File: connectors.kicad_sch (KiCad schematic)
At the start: 4 parts, among them J1 Conn_01x05_Pin, J2 Conn_01x05_Pin, J3 Conn_01x09_Pin, J4 Conn_02x03_Odd_Even

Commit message: Values Added
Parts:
- renumbered J3 to J2, J2 to J3
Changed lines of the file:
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@@
 		(on_board yes)
 		(dnp no)
-		(property "Reference" "J3"
+		(property "Reference" "J2"
 			(at 112.395 99.06 0)
 			(effects
@@
 			(project ""
 				(path "/9a58bdc0-cf43-4f46-bdf9-3019f1d018de/dbde1bf3-31e8-43a9-a1f1-c0653e04f173"
-					(reference "J3")
+					(reference "J2")
 					(unit 1)
 				)
@@
 		(on_board yes)
 		(dnp no)
-		(property "Reference" "J2"
+		(property "Reference" "J3"
 			(at 131.445 72.39 0)
 			(effects
@@
 			(project "MCU_Datalogger"
 				(path "/9a58bdc0-cf43-4f46-bdf9-3019f1d018de/dbde1bf3-31e8-43a9-a1f1-c0653e04f173"
-					(reference "J2")
+					(reference "J3")
 					(unit 1)
 				)

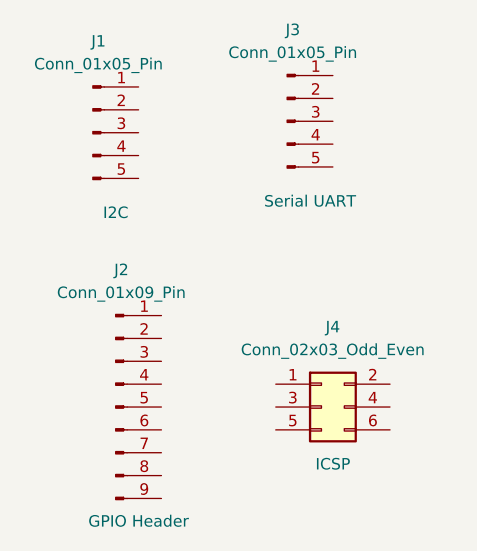
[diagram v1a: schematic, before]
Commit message: Problems in connectors fixed
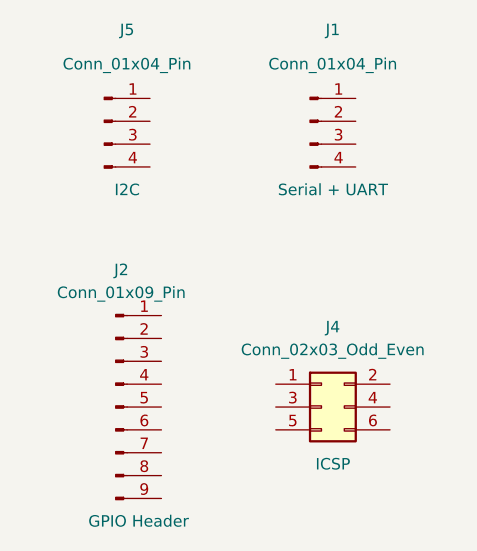
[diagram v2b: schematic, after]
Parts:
- removed J1, J3: Conn_01x05_Pin, symbol Connector:Conn_01x05_Pin
- added J1, J5: Conn_01x04_Pin, symbol Connector:Conn_01x04_Pin
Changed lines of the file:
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@@
+	)
+	(symbol
+		(lib_id "Connector:Conn_01x04_Pin")
+		(at 133.35 82.55 0)
+		(unit 1)
+		(exclude_from_sim no)
+		(in_bom yes)
+		(on_board yes)
+		(dnp no)
+		(property "Reference" "J1"
+			(at 135.89 72.39 0)
+			(effects
+				(font
+					(size 1.27 1.27)
+				)
+			)
+		)
+		(property "Value" "Conn_01x04_Pin"
+			(at 135.89 76.2 0)
+			(effects
+				(font
+					(size 1.27 1.27)
+				)
+			)
+		)
+		(property "Footprint" ""
+			(at 133.35 82.55 0)
+			(effects
+				(font
+					(size 1.27 1.27)
+				)
+				(hide yes)
+			)
+		)
+		(property "Datasheet" "~"
+			(at 133.35 82.55 0)
+			(effects
+				(font
+					(size 1.27 1.27)
+				)
+				(hide yes)
+			)
+		)
+		(property "Description" "Generic connector, single row, 01x04, script generated"
+			(at 133.35 82.55 0)
+			(effects
+				(font
+					(size 1.27 1.27)
+				)
+				(hide yes)
+			)
+		)
+		(property "Purpose" "Serial + UART"
+			(at 135.89 90.17 0)
+			(effects
+				(font
+					(size 1.27 1.27)
+				)
+			)
+		)
+		(pin "3"
+		)
+		(pin "2"
+		)
+		(pin "4"
+		)
+		(pin "1"
+		)
+		(instances
+			(project "MCU_Datalogger"
+				(path "/9a58bdc0-cf43-4f46-bdf9-3019f1d018de/dbde1bf3-31e8-43a9-a1f1-c0653e04f173"
+					(reference "J1")
+					(unit 1)
+				)
+			)
+		)
+	)
+	(symbol
+		(lib_id "Connector:Conn_01x04_Pin")
+		(at 110.49 82.55 0)
+		(unit 1)
+		(exclude_from_sim no)
+		(in_bom yes)
+		(on_board yes)
+		(dnp no)
+		(property "Reference" "J5"
+			(at 113.03 72.39 0)
+			(effects
+				(font
+					(size 1.27 1.27)
+				)
+			)
+		)
+		(property "Value" "Conn_01x04_Pin"
+			(at 113.03 76.2 0)
+			(effects
+				(font
+					(size 1.27 1.27)
+				)
+			)
+		)
+		(property "Footprint" ""
+			(at 110.49 82.55 0)
+			(effects
+				(font
+					(size 1.27 1.27)
+				)
+				(hide yes)
+			)
+		)
+		(property "Datasheet" "~"
+			(at 110.49 82.55 0)
+			(effects
+				(font
+					(size 1.27 1.27)
+				)
+				(hide yes)
+			)
+		)
+		(property "Description" "Generic connector, single row, 01x04, script generated"
+			(at 110.49 82.55 0)
+			(effects
+				(font
+					(size 1.27 1.27)
+				)
+				(hide yes)
+			)
+		)
+		(property "Purpose" "I2C"
+			(at 113.03 90.17 0)
+			(effects
+				(font
+					(size 1.27 1.27)
+				)
+			)
+		)
+		(pin "3"
+		)
+		(pin "2"
+		)
+		(pin "4"
+		)
+		(pin "1"
+		)
+		(instances
+			(project ""
+				(path "/9a58bdc0-cf43-4f46-bdf9-3019f1d018de/dbde1bf3-31e8-43a9-a1f1-c0653e04f173"
+					(reference "J5")
+					(unit 1)
+				)
+			)
+		)
 	)
 	(symbol
@@
 					(unit 1)
 				)
-			)
-		)
-	)
-	(symbol
-		(lib_id "Connector:Conn_01x05_Pin")
-		(at 109.22 83.82 0)
-		(unit 1)
-		(exclude_from_sim no)
-		(in_bom yes)
-		(on_board yes)
-		(dnp no)
-		(property "Reference" "J1"
-			(at 109.855 73.66 0)
-			(effects
-				(font
-					(size 1.27 1.27)
-				)
-			)
-		)
-		(property "Value" "Conn_01x05_Pin"
-			(at 109.855 76.2 0)
-			(effects
-				(font
-					(size 1.27 1.27)
-				)
-			)
-		)
-		(property "Footprint" ""
-			(at 109.22 83.82 0)
-			(effects
-				(font
-					(size 1.27 1.27)
-				)
-				(hide yes)
-			)
-		)
-		(property "Datasheet" "~"
-			(at 109.22 83.82 0)
-			(effects
-				(font
-					(size 1.27 1.27)
-				)
-				(hide yes)
-			)
-		)
-		(property "Description" "Generic connector, single row, 01x05, script generated"
-			(at 109.22 83.82 0)
-			(effects
-				(font
-					(size 1.27 1.27)
-				)
-				(hide yes)
-			)
-		)
-		(property "Purpose" "I2C"
-			(at 111.76 92.71 0)
-			(effects
-				(font
-					(size 1.27 1.27)
-				)
-			)
-		)
-		(pin "4"
-		)
-		(pin "1"
-		)
-		(pin "2"
-		)
-		(pin "3"
-		)
-		(pin "5"
-		)
-		(instances
-			(project ""
-				(path "/9a58bdc0-cf43-4f46-bdf9-3019f1d018de/dbde1bf3-31e8-43a9-a1f1-c0653e04f173"
-					(reference "J1")
-					(unit 1)
-				)
-			)
-		)
-	)
-	(symbol
-		(lib_id "Connector:Conn_01x05_Pin")
-		(at 130.81 82.55 0)
-		(unit 1)
-		(exclude_from_sim no)
-		(in_bom yes)
-		(on_board yes)
-		(dnp no)
-		(property "Reference" "J3"
-			(at 131.445 72.39 0)
-			(effects
-				(font
-					(size 1.27 1.27)
-				)
-			)
-		)
-		(property "Value" "Conn_01x05_Pin"
-			(at 131.445 74.93 0)
-			(effects
-				(font
-					(size 1.27 1.27)
-				)
-			)
-		)
-		(property "Footprint" ""
-			(at 130.81 82.55 0)
-			(effects
-				(font
-					(size 1.27 1.27)
-				)
-				(hide yes)
-			)
-		)
-		(property "Datasheet" "~"
-			(at 130.81 82.55 0)
-			(effects
-				(font
-					(size 1.27 1.27)
-				)
-				(hide yes)
-			)
-		)
-		(property "Description" "Generic connector, single row, 01x05, script generated"
-			(at 130.81 82.55 0)
-			(effects
-				(font
-					(size 1.27 1.27)
-				)
-				(hide yes)
-			)
-		)
-		(property "Purpose" "Serial UART"
-			(at 133.35 91.44 0)
-			(effects
-				(font
-					(size 1.27 1.27)
-				)
-			)
-		)
-		(pin "4"
-		)
-		(pin "1"
-		)
-		(pin "2"
-		)
-		(pin "3"
-		)
-		(pin "5"
-		)
-		(instances
-			(project "MCU_Datalogger"
-				(path "/9a58bdc0-cf43-4f46-bdf9-3019f1d018de/dbde1bf3-31e8-43a9-a1f1-c0653e04f173"
-					(reference "J3")
-					(unit 1)
-				)

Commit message: Symbol to Footprint Association
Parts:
- J1, J5: footprint (none) -> Connector_PinHeader_2.54mm:PinHeader_1x04_P2.54mm_Vertical
- J2: footprint (none) -> Connector_PinHeader_2.54mm:PinHeader_1x09_P2.54mm_Vertical_SMD_Pin1Left
- J4: footprint (none) -> Connector_PinHeader_2.54mm:PinHeader_2x03_P2.54mm_Vertical
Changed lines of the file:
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@@
 			)
 		)
-		(property "Footprint" ""
+		(property "Footprint" "Connector_PinHeader_2.54mm:PinHeader_2x03_P2.54mm_Vertical"
 			(at 134.62 114.3 0)
 			(effects
@@
 			)
 		)
-		(property "Footprint" ""
+		(property "Footprint" "Connector_PinHeader_2.54mm:PinHeader_1x04_P2.54mm_Vertical"
 			(at 133.35 82.55 0)
 			(effects
@@
 			)
 		)
-		(property "Footprint" ""
+		(property "Footprint" "Connector_PinHeader_2.54mm:PinHeader_1x04_P2.54mm_Vertical"
 			(at 110.49 82.55 0)
 			(effects
@@
 			)
 		)
-		(property "Footprint" ""
+		(property "Footprint" "Connector_PinHeader_2.54mm:PinHeader_1x09_P2.54mm_Vertical_SMD_Pin1Left"
 			(at 111.76 114.3 0)
 			(effects

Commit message: Wiring done
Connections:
- net MISO: now reaches J4.1 (Pin_1)
- net Vcc: now reaches J4.2 (Pin_2)
- net Vcc: now also J1.2 (Pin_2), J2.9 (Pin_9), J5.2 (Pin_2)
- net SCK: now reaches J4.3 (Pin_3)
- net SCK: now also J5.4 (Pin_4)
- net MOSI: now reaches J4.4 (Pin_4)
- net RESET: now reaches J4.5 (Pin_5)
- net GND: now reaches J4.6 (Pin_6)
- net GND: now also J1.1 (Pin_1), J2.8 (Pin_8), J5.1 (Pin_1)
- net RX: now reaches J1.3 (Pin_3)
- net TX: now reaches J1.4 (Pin_4)
- net SDA: now reaches J5.3 (Pin_3)
- net D2: now reaches J2.1 (Pin_1)
- net D3: now reaches J2.2 (Pin_2)
- net D4: now reaches J2.3 (Pin_3)
- net D5: now reaches J2.4 (Pin_4)
- net D6: now reaches J2.5 (Pin_5)
- net D7: now reaches J2.6 (Pin_6)
- net D8: now reaches J2.7 (Pin_7)
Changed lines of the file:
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@@
 	(generator_version "9.0")
 	(paper "A4")
+	(hierarchical_label "GND"
+		(shape passive)
+		(at 138.43 80.01 0)
+		(effects
+			(font
+				(size 1.27 1.27)
+			)
+			(justify left)
+		)
+	)
+	(hierarchical_label "GND"
+		(shape passive)
+		(at 142.24 116.84 0)
+		(effects
+			(font
+				(size 1.27 1.27)
+			)
+			(justify left)
+		)
+	)
+	(hierarchical_label "D5"
+		(shape bidirectional)
+		(at 116.84 111.76 0)
+		(effects
+			(font
+				(size 1.27 1.27)
+			)
+			(justify left)
+		)
+	)
+	(hierarchical_label "GND"
+		(shape passive)
+		(at 115.57 80.01 0)
+		(effects
+			(font
+				(size 1.27 1.27)
+			)
+			(justify left)
+		)
+	)
+	(hierarchical_label "GND"
+		(shape passive)
+		(at 116.84 121.92 0)
+		(effects
+			(font
+				(size 1.27 1.27)
+			)
+			(justify left)
+		)
+	)
+	(hierarchical_label "D3"
+		(shape bidirectional)
+		(at 116.84 106.68 0)
+		(effects
+			(font
+				(size 1.27 1.27)
+			)
+			(justify left)
+		)
+	)
+	(hierarchical_label "SCK"
+		(shape passive)
+		(at 129.54 114.3 180)
+		(effects
+			(font
+				(size 1.27 1.27)
+			)
+			(justify right)
+		)
+	)
+	(hierarchical_label "SCK"
+		(shape passive)
+		(at 115.57 87.63 0)
+		(effects
+			(font
+				(size 1.27 1.27)
+			)
+			(justify left)
+		)
+	)
+	(hierarchical_label "Vcc"
+		(shape passive)
+		(at 138.43 82.55 0)
+		(effects
+			(font
+				(size 1.27 1.27)
+			)
+			(justify left)
+		)
+	)
+	(hierarchical_label "MOSI"
+		(shape input)
+		(at 142.24 114.3 0)
+		(effects
+			(font
+				(size 1.27 1.27)
+			)
+			(justify left)
+		)
+	)
+	(hierarchical_label "TX"
+		(shape output)
+		(at 138.43 87.63 0)
+		(effects
+			(font
+				(size 1.27 1.27)
+			)
+			(justify left)
+		)
+	)
+	(hierarchical_label "D8"
+		(shape bidirectional)
+		(at 116.84 119.38 0)
+		(effects
+			(font
+				(size 1.27 1.27)
+			)
+			(justify left)
+		)
+	)
+	(hierarchical_label "Vcc"
+		(shape passive)
+		(at 142.24 111.76 0)
+		(effects
+			(font
+				(size 1.27 1.27)
+			)
+			(justify left)
+		)
+	)
+	(hierarchical_label "D4"
+		(shape bidirectional)
+		(at 116.84 109.22 0)
+		(effects
+			(font
+				(size 1.27 1.27)
+			)
+			(justify left)
+		)
+	)
+	(hierarchical_label "D2"
+		(shape bidirectional)
+		(at 116.84 104.14 0)
+		(effects
+			(font
+				(size 1.27 1.27)
+			)
+			(justify left)
+		)
+	)
+	(hierarchical_label "RX"
+		(shape input)
+		(at 138.43 85.09 0)
+		(effects
+			(font
+				(size 1.27 1.27)
+			)
+			(justify left)
+		)
+	)
+	(hierarchical_label "D7"
+		(shape bidirectional)
+		(at 116.84 116.84 0)
+		(effects
+			(font
+				(size 1.27 1.27)
+			)
+			(justify left)
+		)
+	)
+	(hierarchical_label "SDA"
+		(shape bidirectional)
+		(at 115.57 85.09 0)
+		(effects
+			(font
+				(size 1.27 1.27)
+			)
+			(justify left)
+		)
+	)
+	(hierarchical_label "Vcc"
+		(shape passive)
+		(at 115.57 82.55 0)
+		(effects
+			(font
+				(size 1.27 1.27)
+			)
+			(justify left)
+		)
+	)
+	(hierarchical_label "D6"
+		(shape bidirectional)
+		(at 116.84 114.3 0)
+		(effects
+			(font
+				(size 1.27 1.27)
+			)
+			(justify left)
+		)
+	)
+	(hierarchical_label "Vcc"
+		(shape passive)
+		(at 116.84 124.46 0)
+		(effects
+			(font
+				(size 1.27 1.27)
+			)
+			(justify left)
+		)
+	)
+	(hierarchical_label "MISO"
+		(shape output)
+		(at 129.54 111.76 180)
+		(effects
+			(font
+				(size 1.27 1.27)
+			)
+			(justify right)
+		)
+	)
+	(hierarchical_label "RESET"
+		(shape passive)
+		(at 129.54 116.84 180)
+		(effects
+			(font
+				(size 1.27 1.27)
+			)
+			(justify right)
+		)
+	)
 	(symbol
 		(lib_id "Connector_Generic:Conn_02x03_Odd_Even")

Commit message: Problem in 9 pin connector
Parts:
- J2: footprint Connector_PinHeader_2.54mm:PinHeader_1x09_P2.54mm_Vertical_SMD_Pin1Left -> Connector_PinHeader_2.54mm:PinHeader_1x09_P2.54mm_Vertical
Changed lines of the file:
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@@
 			)
 		)
-		(property "Footprint" "Connector_PinHeader_2.54mm:PinHeader_1x09_P2.54mm_Vertical_SMD_Pin1Left"
+		(property "Footprint" "Connector_PinHeader_2.54mm:PinHeader_1x09_P2.54mm_Vertical"
 			(at 111.76 114.3 0)
 			(effects
